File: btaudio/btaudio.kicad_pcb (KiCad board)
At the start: 2 copper layers, 22 x 51 mm, 52 parts, among them J1 BAT_CON, J2 USB_C_Receptacle_USB2.0_16P, J4 AudioJack4, SW1 POWER_SW, SW2 PLAY/VOL+, SW3 PAUSE/VOL-, SW4 PREV/BT PAIRING, SW5 NEXT/BT DISCONNECT, SW6 SOFT RESET, U1 EWM104-BT5125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

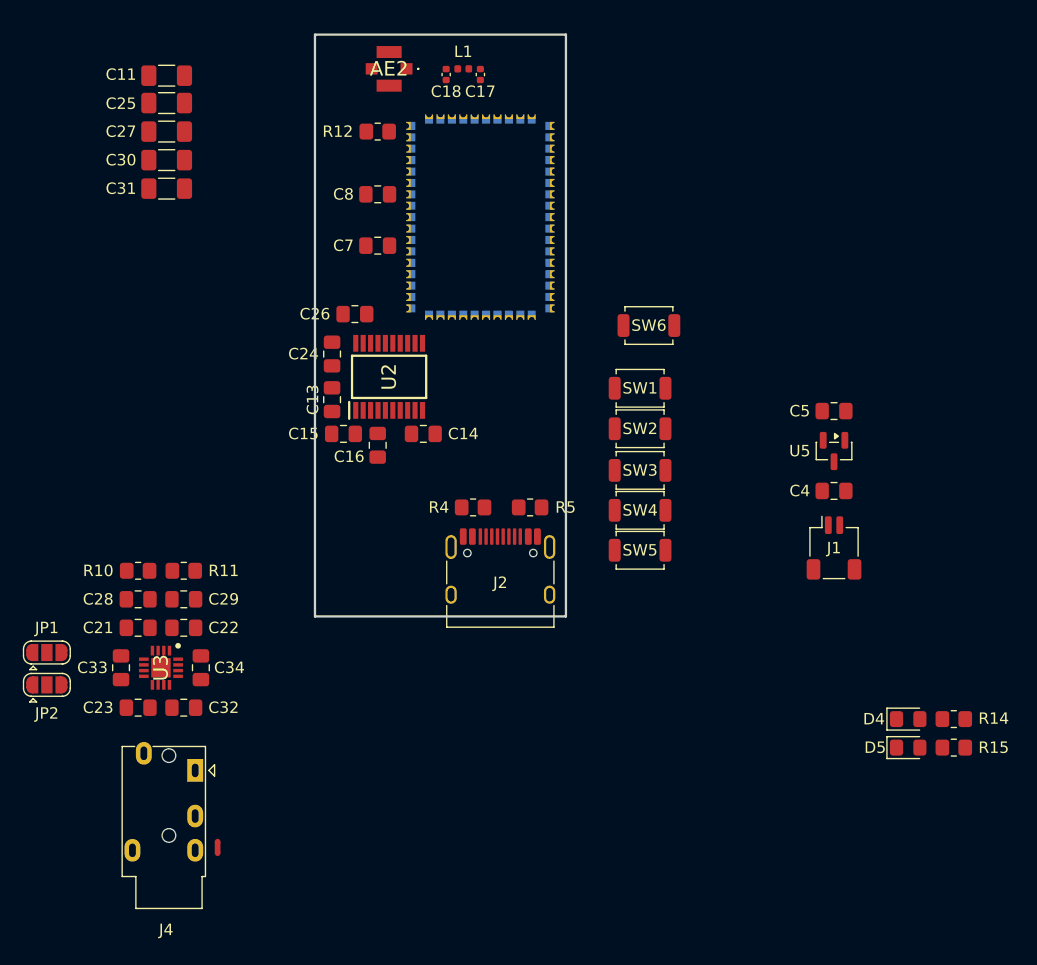
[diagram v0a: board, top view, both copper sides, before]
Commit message: compacting layout
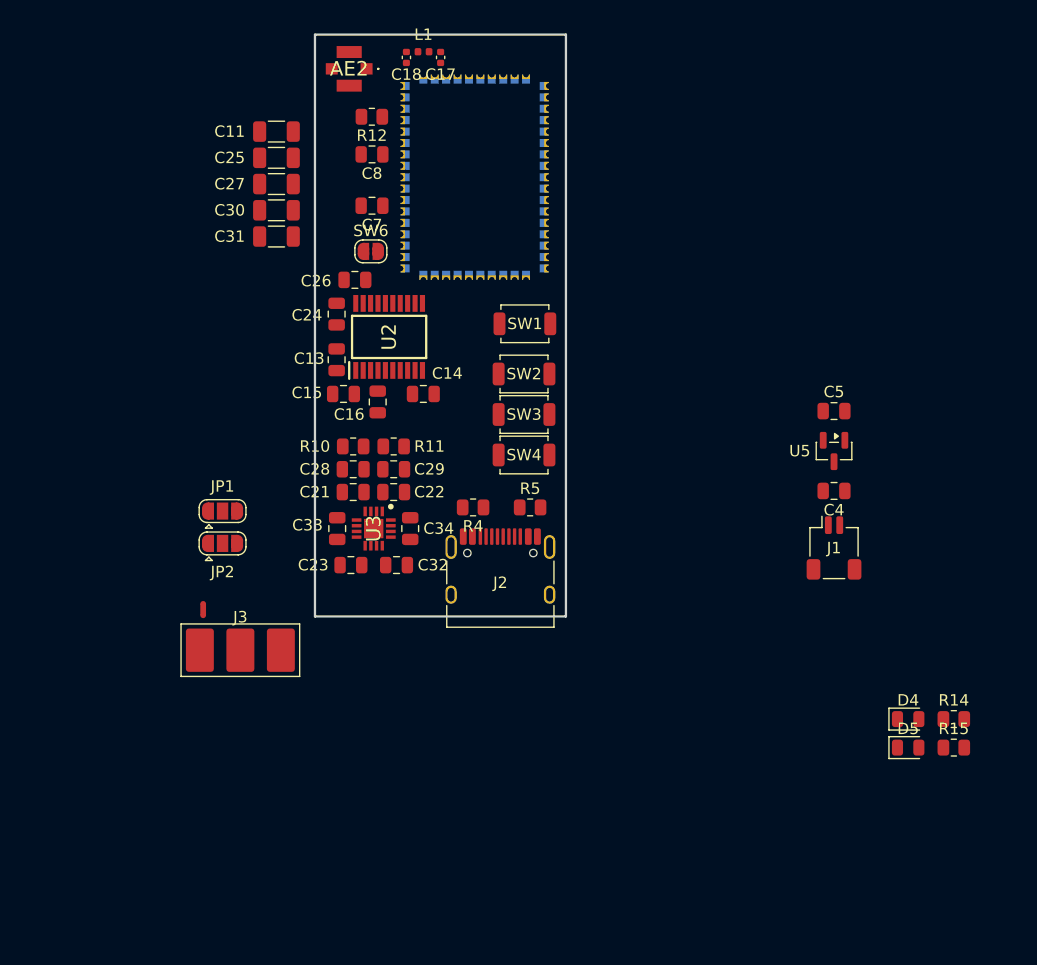
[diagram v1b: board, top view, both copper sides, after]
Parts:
- removed J4: AudioJack4, Connector_Audio:Jack_3.5mm_PJ320E_Horizontal
- removed SW5: NEXT/BT DISCONNECT, Button_Switch_SMD:SW_SPST_TS-1088-xR020
- added J3: Audio, PCM_Crystal_Handsoldering_AKL:Resonator_SMD-3Pin_7.2x3.0mm_BigPads, F.Cu at (125.0, 132.0)
- C11, C25, C27, C30, C31: footprint Capacitor_SMD:C_1206_3216Metric_Pad1.33x1.80mm_HandSolder -> Capacitor_SMD:C_1206_3216Metric
- C13, C14, C15, C16, C21, C22, C23, C24, C26, C28, C29, C32, C33, C34, C4, C5, C7, C8: footprint Capacitor_SMD:C_0805_2012Metric_Pad1.18x1.45mm_HandSolder -> Capacitor_SMD:C_0805_2012Metric
- D4, D5: footprint LED_SMD:LED_0805_2012Metric_Pad1.15x1.40mm_HandSolder -> LED_SMD:LED_0805_2012Metric
- R10, R11, R12, R14, R15, R4, R5: footprint Resistor_SMD:R_0805_2012Metric_Pad1.20x1.40mm_HandSolder -> Resistor_SMD:R_0805_2012Metric
- SW6: footprint Button_Switch_SMD:SW_SPST_TS-1088-xR020 -> Jumper:SolderJumper-2_P1.3mm_Open_RoundedPad1.0x1.5mm
- moved SW6 25.2 mm to (136.4, 97.0)
- moved C33 22.5 mm to (133.4, 121.3)
- moved C23 22.5 mm to (134.7, 124.5)
- moved C32 22.5 mm to (138.7, 124.5)
- moved C21 22.3 mm to (134.8, 118.1)
- moved U3 22.3 mm to (136.7, 121.3)
- moved C34 22.0 mm to (139.8, 121.3)
- moved C28 22.0 mm to (134.8, 116.1)
- moved C22 21.9 mm to (138.4, 118.1)
- moved R10 21.8 mm to (134.8, 114.1)
- moved C29 21.6 mm to (138.4, 116.1)
- moved R11 21.4 mm to (138.4, 114.1)
- moved NT1 20.9 mm to (121.7, 128.4)
- moved JP2 19.8 mm to (123.4, 122.6)
- moved JP1 19.8 mm to (123.4, 119.8)
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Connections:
- U1 pad 28: Net-(U1-PIO[5]) -> unconnected-(U1-PIO[5]-Pad28)

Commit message: primary layout done
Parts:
- removed SW2: PLAY/VOL+, Button_Switch_SMD:SW_SPST_TS-1088-xR020
- removed SW3: PAUSE/VOL-, Button_Switch_SMD:SW_SPST_TS-1088-xR020
- removed SW4: PREV/BT PAIRING, Button_Switch_SMD:SW_SPST_TS-1088-xR020
- added J6: Battery, Connector_PinHeader_2.54mm:PinHeader_1x02_P2.54mm_Vertical, F.Cu at (146.7, 107.2)
- J1: value BAT_CON -> BTNS; footprint Connector_JST:JST_SH_SM02B-SRSS-TB_1x02-1MP_P1.00mm_Horizontal -> Connector_PinHeader_2.54mm:PinHeader_1x04_P2.54mm_Vertical
- J3: footprint PCM_Crystal_Handsoldering_AKL:Resonator_SMD-3Pin_7.2x3.0mm_BigPads -> Aux-Pads:aux-pads
- JP1, JP2: moved to B.Cu
- moved R14 48.3 mm to (146.8, 111.9), turned to 90 degrees
- moved R15 48.2 mm to (148.7, 111.9), turned to 90 degrees
- moved D4 43.1 mm to (146.8, 115.3), turned to 90 degrees
- moved D5 42.9 mm to (148.7, 115.3), turned to 90 degrees
- moved C4 34.2 mm to (143.7, 110.3)
- moved C5 33.9 mm to (143.5, 116.5), turned to 180 degrees
- moved U5 33.5 mm to (143.5, 113.4), turned to 90 degrees
- moved J1 29.7 mm to (151.5, 107.8)
- moved JP1 15.2 mm to (138.6, 120.2), turned to 180 degrees
- moved JP2 15.2 mm to (138.6, 123.0), turned to 180 degrees
- moved NT1 15.0 mm to (136.5, 126.0), turned to 0 degrees
- moved J3 12.3 mm to (136.5, 127.6)
- moved SW6 9.45 mm to (144.6, 101.7)
- moved C31 5.97 mm to (134.0, 96.9)
- moved C30 5.96 mm to (134.0, 94.5)
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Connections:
- J1 pad 2: /VBAT -> Net-(J1-Pin_2)
- U1 pad 25: Net-(U1-PIO[4]) -> Net-(J1-Pin_4)
- U1 pad 26: Net-(U1-PIO[3]) -> Net-(J1-Pin_3)
- U1 pad 31: Net-(U1-PIO[2]) -> Net-(J1-Pin_2)
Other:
- board text added: "L"
- board text added: "R"

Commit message: layout almost done v1
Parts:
- NT1: moved to B.Cu
- U1: footprint EWM104-BT5125-PCB:EWM104-BT5125(KiCAD) -> EWM104-BT5125-PCB:EWM104-BT5125(KiCAD)_flipped_nonhole
- moved JP1 6.06 mm to (132.9, 118.1), turned to -90 degrees
- moved JP2 5.78 mm to (132.9, 124.2), turned to 90 degrees
- moved SW1 1.05 mm to (149.9, 102.3)
- moved R5 0.50 mm to (150.4, 119.8)
- moved C34 0.45 mm to (140.3, 121.3)
- moved C33 0.45 mm to (133.0, 121.3)
- moved C5 0.41 mm to (143.1, 116.6)
- moved U5 0.41 mm to (143.1, 113.5)
- moved R4 0.20 mm to (145.3, 119.8)
- turned C23 to 180 degrees
- turned NT1 to 180 degrees
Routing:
- net /VIN: track 0.00 -> 65.6 mm, vias 0 -> 3
- net /AMP_EN: track 0.00 -> 48.3 mm, vias 0 -> 3
- net /VBAT: track 0.00 -> 46.7 mm, vias 0 -> 3
- net /D-: track 0.00 -> 42.2 mm, vias 0 -> 2
- net /D+: track 0.00 -> 41.2 mm, vias 0 -> 2
- net GND: track 0.00 -> 34.8 mm, vias 0 -> 32
- net /+3V3: track 0.00 -> 26.5 mm, vias 0 -> 12
- net Net-(U1-AIO[0]/LED[0]): track 0.00 -> 24.8 mm, vias 0 -> 2
- net Net-(U1-AIO[1]/LED[1]): track 0.00 -> 23.6 mm, vias 0 -> 2
- net /I2S_SDATA: track 0.00 -> 20.3 mm, vias 0 -> 2
- net Net-(U1-SYS_CTRL): track 0.00 -> 19.4 mm, vias 0 -> 2
- net /I2S_SCK: track 0.00 -> 18.8 mm, vias 0 -> 2
- net /I2S_LRCK: track 0.00 -> 18.0 mm, vias 0 -> 2
- net Net-(J1-Pin_2): track 0.00 -> 17.2 mm, vias 0 -> 1
- net Net-(J1-Pin_4): track 0.00 -> 17.2 mm
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- added copper zone on In2.Cu, net /+3V3
- added copper zone on B.Cu, net GND
- added copper zone on F.Cu, net GND
- added copper zone on In1.Cu, net GND
- added copper zone on In2.Cu, net GND
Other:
- copper layers 2 -> 4

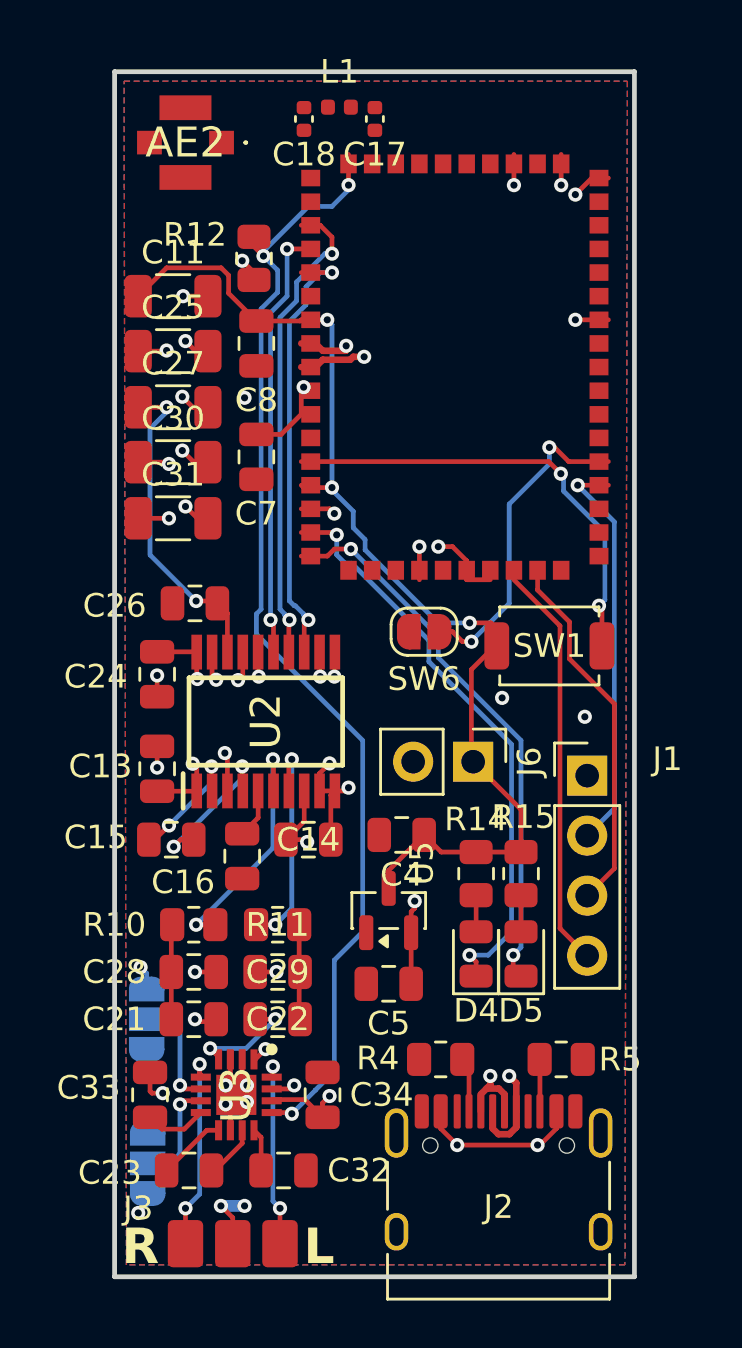
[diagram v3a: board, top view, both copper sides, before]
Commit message: wiring done
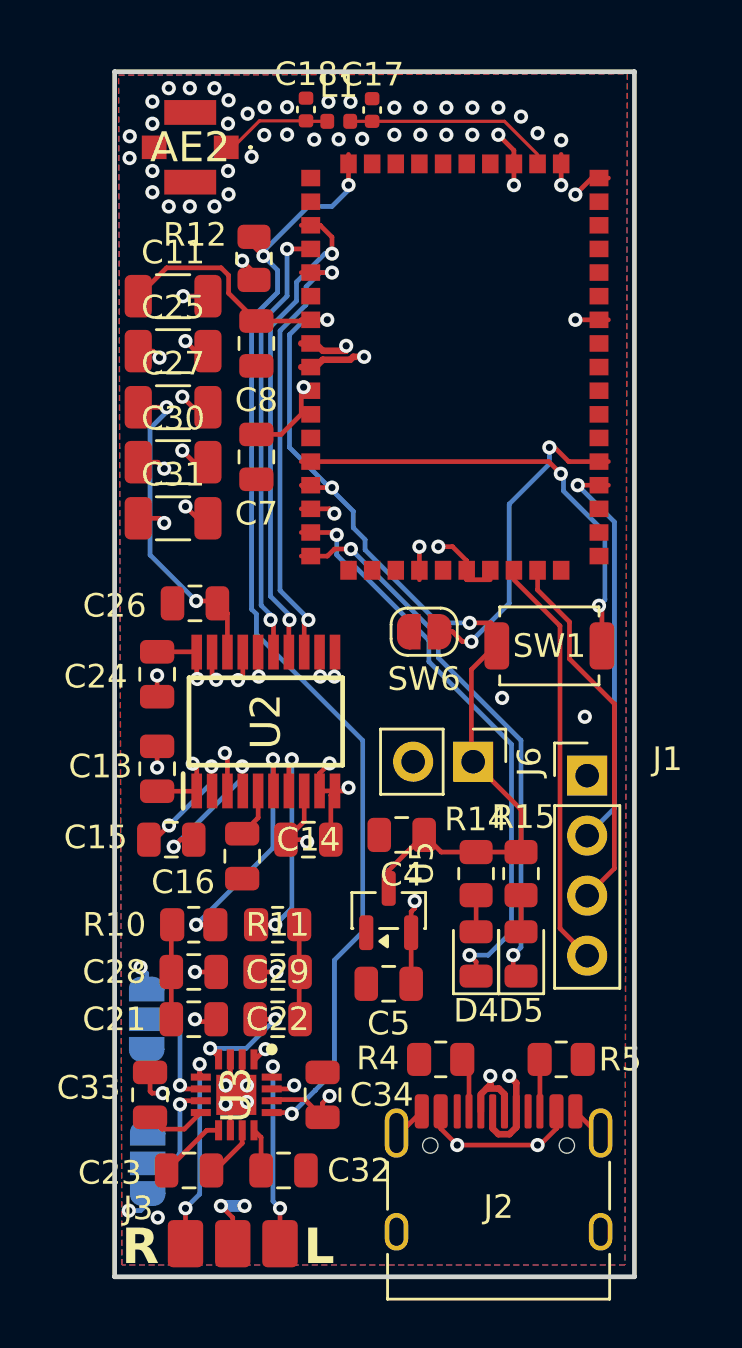
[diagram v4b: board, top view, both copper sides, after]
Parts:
- moved L1 0.60 mm to (141.0, 80.1)
- moved C18 0.41 mm to (139.6, 79.6), turned to 90 degrees
- moved C17 0.40 mm to (142.4, 79.6), turned to 90 degrees
- moved AE2 0.28 mm to (134.7, 81.2)
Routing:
- net Net-(U1-ANT): track 0.00 -> 8.51 mm
- net Net-(AE2-A): track 0.00 -> 4.75 mm
- net GND: track 34.8 -> 38.8 mm, vias 32 -> 72
- net /VBAT: track 46.7 -> 48.6 mm
- net /VIN: track 65.6 -> 64.3 mm
